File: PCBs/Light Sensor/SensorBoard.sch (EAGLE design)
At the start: 29 parts, among them J1 AVR_SPI_PRG_6PTH

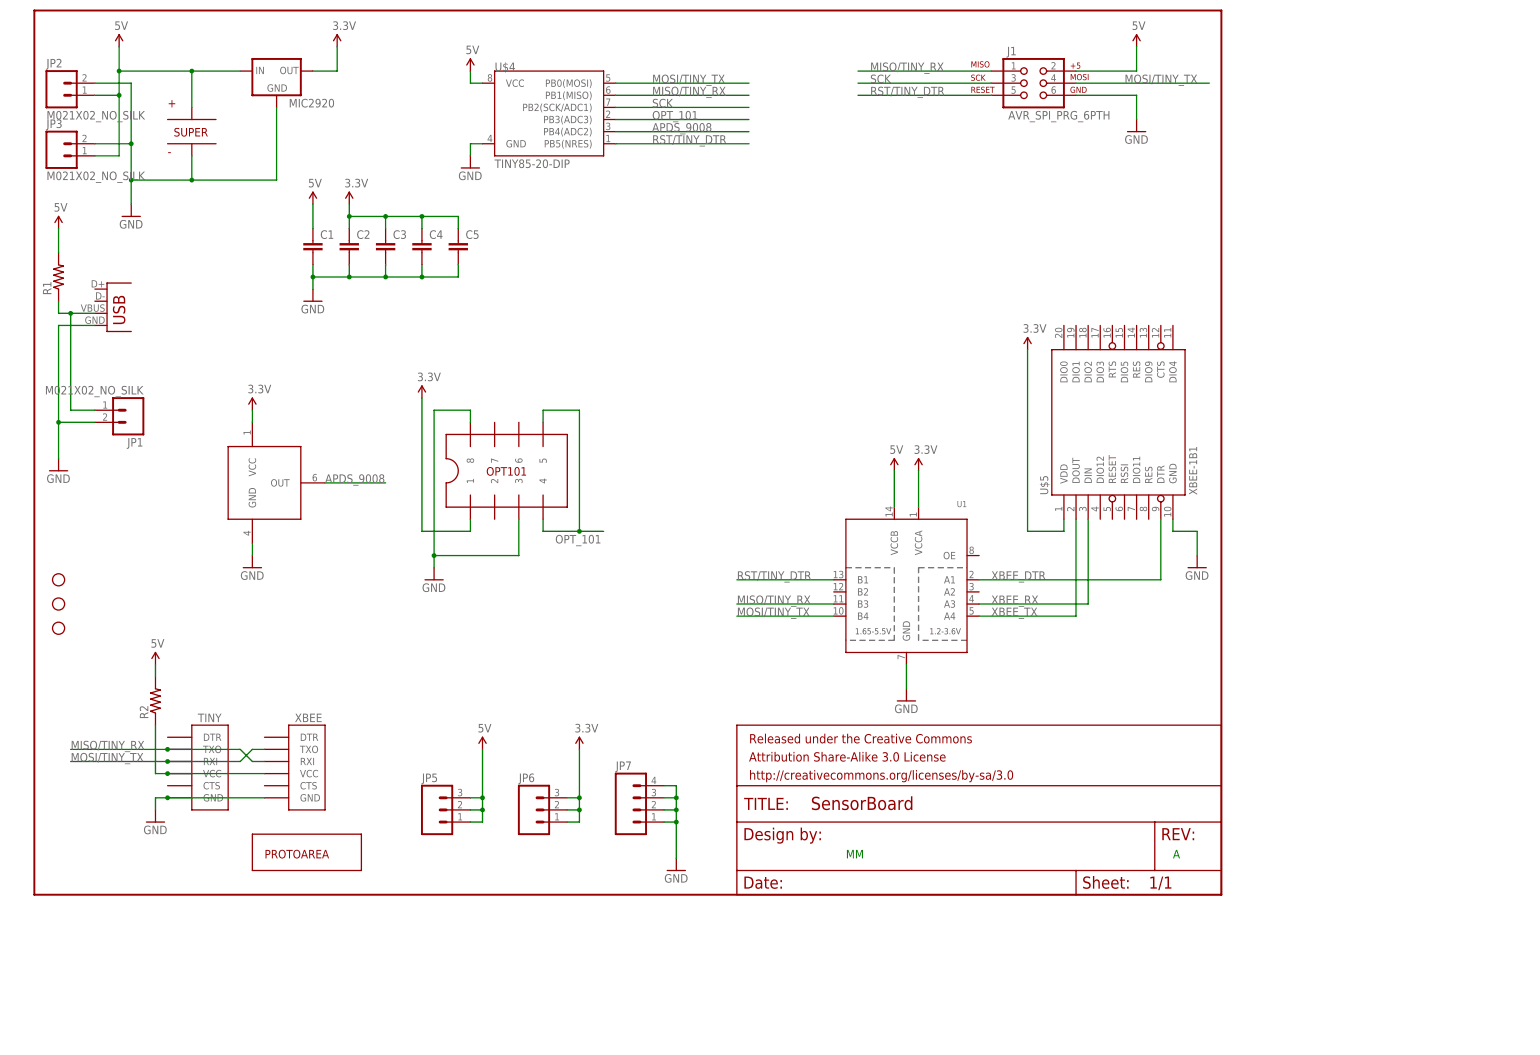
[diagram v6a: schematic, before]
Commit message: Fixes:   - Changed to ATTiny84 for more pins   - Changed to enable/disable 3.3v LDO to avoid droop conditions
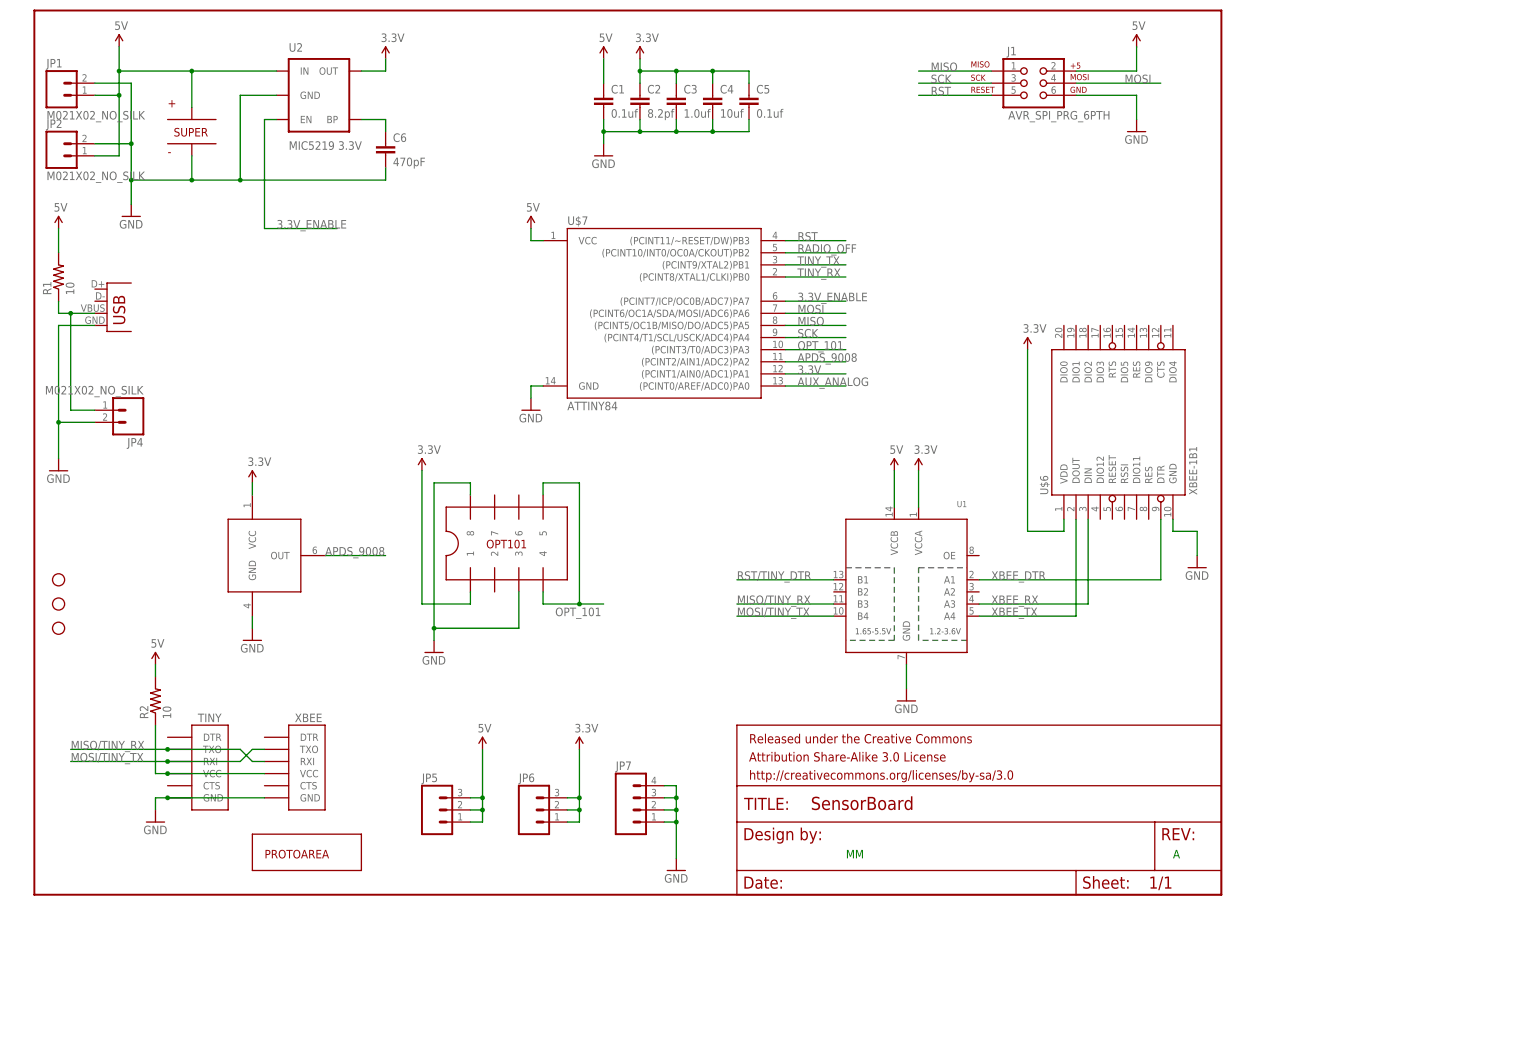
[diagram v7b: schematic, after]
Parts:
- removed MIC2920: V_REG_MIC2920, SparkFun-PowerIC:V_REG_MIC2920
- removed U$8: PROTOAREA-10X10, MyLibrary:PROTOAREA-10X10
- added C6: 470pF, SparkFun-Capacitors:CAP1210
- added U$2: APDS-9008, MyLibrary:APDS-9008
- added U2: MIC5219 3.3V, SparkFun-PowerIC:V_REG_MIC52193.3V
- C1, C5: value (none) -> 0.1uf
- C2: value (none) -> 8.2pf
- C3: value (none) -> 1.0uf
- C4: value (none) -> 10uf
- JP3: value M021X02_NO_SILK -> USBSMD; device SparkFun-Connectors:M021X02_NO_SILK -> SparkFun-Connectors:USBSMD
- JP4: value USBSMD -> M021X02_NO_SILK; device SparkFun-Connectors:USBSMD -> SparkFun-Connectors:M021X02_NO_SILK
- R1, R2: value (none) -> 10
- U$1: value OPT101TH -> FYD0H225ZF; device MyLibrary:OPT101TH -> MyLibrary:FYD0H225ZF
- U$3: value APDS-9008 -> PROTOAREA-10X10; device MyLibrary:APDS-9008 -> MyLibrary:PROTOAREA-10X10
- U$4: value TINY85-20-DIP -> OPT101TH; device SparkFun-DigitalIC:ATTINY45TINY85-20-DIP -> MyLibrary:OPT101TH
- U$7: value FYD0H225ZF -> ATTINY84; device MyLibrary:FYD0H225ZF -> SparkFun-DigitalIC:ATTINY84
- renumbered U$5 to U$6
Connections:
- new net 3.3V_ENABLE: U$7.(PCINT7/ICP/OC0B/ADC7)PA7, U2.EN
- new net AUX_ANALOG: U$7.(PCINT0/AREF/ADC0)PA0
- new net MISO: J1.1, U$7.(PCINT5/OC1B/MISO/DO/ADC5)PA5
- new net MOSI: J1.4, U$7.(PCINT6/OC1A/SDA/MOSI/ADC6)PA6
- new net N$3: C6.1, U2.BP
- new net RADIO_OFF: U$7.(PCINT10/INT0/OC0A/CKOUT)PB2
- new net RST: J1.5, U$7.(PCINT11/~RESET/DW)PB3
- new net TINY_RX: U$7.(PCINT8/XTAL1/CLKI)PB0
- new net TINY_TX: U$7.(PCINT9/XTAL2)PB1
- net 3.3V: now also U$2.VCC, U$4.1, U$7.(PCINT1/AIN0/ADC1)PA1, U2.OUT; no longer MIC2920.OUT, U$1.1, U$3.VCC
- net 5V: now also JP1.1, U$1.+, U$7.VCC, U2.IN; no longer JP3.1, MIC2920.IN, U$4.VCC, U$7.+
- net APDS_9008: now also U$2.OUT, U$7.(PCINT2/AIN1/ADC2)PA2; no longer U$3.OUT, U$4.PB4(ADC2)
- net GND: now also C6.2, JP3.GND, JP4.2, U$1.-, U$2.GND, U$4.3, U$4.8, U$7.GND, U2.GND; no longer JP3.2, JP4.GND, MIC2920.GND, U$1.3, U$1.8, U$3.GND, U$4.GND, U$7.-
- net MISO/TINY_RX: no longer J1.1, U$4.PB1(MISO)
- net MOSI/TINY_TX: no longer J1.4, U$4.PB0(MOSI)
- net N$1: now also JP3.VBUS, JP4.1; no longer JP1.1, JP4.VBUS
- net OPT_101: now also U$4.4, U$4.5, U$7.(PCINT3/T0/ADC3)PA3; no longer U$1.4, U$1.5, U$4.PB3(ADC3)
- net RST/TINY_DTR: no longer J1.5, U$4.PB5(NRES)
- net SCK: now also U$7.(PCINT4/T1/SCL/USCK/ADC4)PA4; no longer U$4.PB2(SCK/ADC1)
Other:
- moved on the sheet: C1, C2, C3, C4, C5, JP1, JP2

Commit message: Working on updates
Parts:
- removed U1: (no value), MyLibrary:TXB0104PWRSOIC14
- added C7, C8: 0.1uf, SparkFun-Capacitors:CAP1210
- added R3: 1k, rcl:R-US_R1210
- added R4: (no value), rcl:R-US_R1210
- added U$5, U$8: SN74LVC2T45, MyLibrary:SN74LVC2T45
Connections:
- removed net MISO/TINY_RX: TINY.TXO, U1.B3, XBEE.RXI
- removed net MOSI/TINY_TX: TINY.RXI, U1.B4, XBEE.TXO
- removed net RST/TINY_DTR: U1.B1
- new net /XBEE_DEBUG: R3.2, R4.2, U$5.DIR
- net 3.3V: now also C7.1, U$5.VB, U$8.VB; no longer U1.VCCA
- net 5V: now also C8.1, R3.1, U$5.VA, U$8.VA; no longer U1.VCCB
- net GND: now also C7.2, C8.2, U$5.GND, U$8.DIR, U$8.GND; no longer U1.GND, XBEE.GND
- net N$2: no longer XBEE.VCC
- net RST: now also R4.1
- net TINY_RX: now also TINY.TXO
- net TINY_TX: now also TINY.RXI
- net XBEE_DTR: now also U$5.B1, XBEE.DTR; no longer U1.A1
- net XBEE_RX: now also U$5.B2, XBEE.TXO; no longer U1.A3
- net XBEE_TX: now also U$8.B1, XBEE.RXI; no longer U1.A4
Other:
- note added: "B"
- note added: "NOTE: DTR normally high. Active low to indicate computer connection."
- note added: "NOTE: Verify FTDI TX/RX direction"
- note removed: "A"
- moved on the sheet: U$6, U$7, XBEE
